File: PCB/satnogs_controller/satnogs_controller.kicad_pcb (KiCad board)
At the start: 2 copper layers, 49.1 x 68 mm, 36 parts, among them P1 RS485, P2 End-Stops, P4 I2C, P5 DC Motors Driver, P6 Power-IN, P7 Motor1, P8 Motor2, P9 Dev-Pins, U1 Pro_Mini, U2 MAX485, U3 POLOLU_A4988, U4 POLOLU_A4988

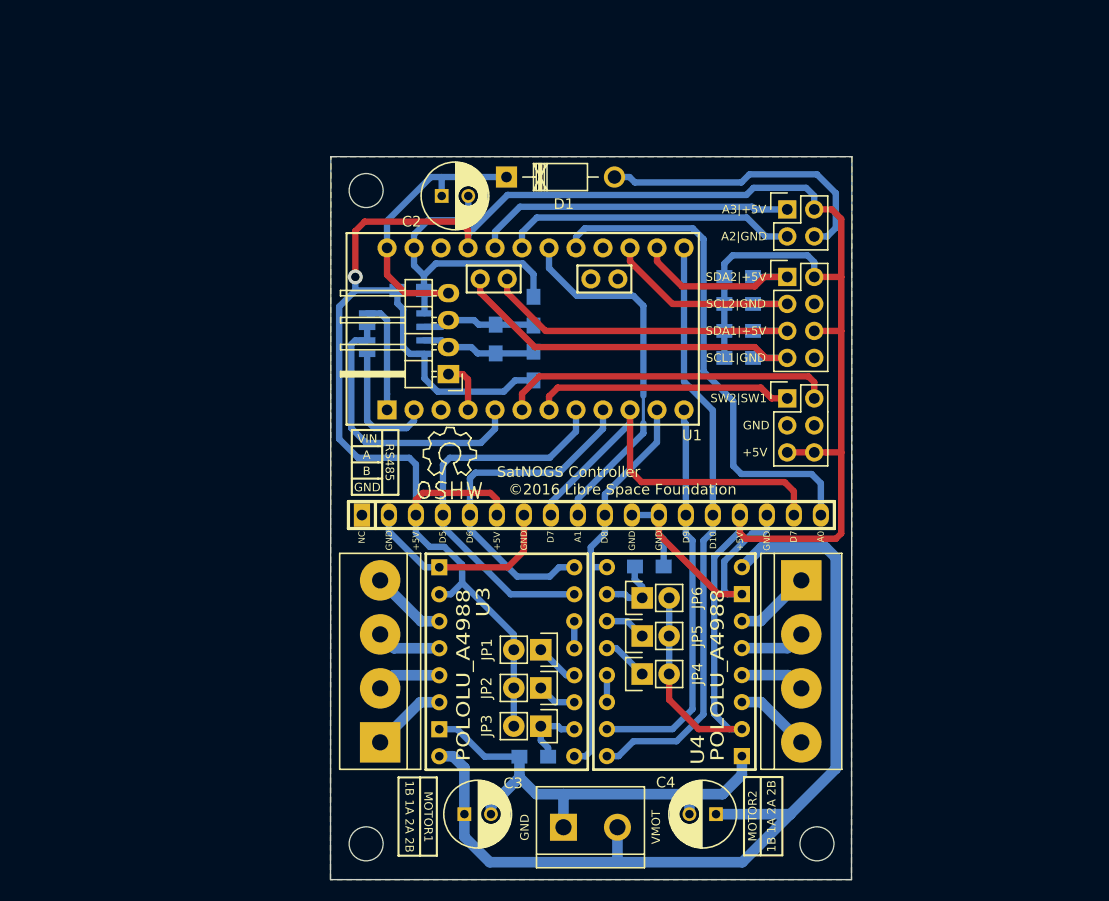
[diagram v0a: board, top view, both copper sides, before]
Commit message: Rotator controller (#27)
* Update satnogs library.

Add new footprints, 3d shapes and schematic components.

* Updates in rotator controller.

Add RJ45 for communication and power in (PoE).
New dimensions of board (euroboard 100x80 mm)
Embed the power supply to the board (WIP).
Add pins for indicator LED and for rf switch (optional).
Add additional pads for power in case that PoE (RJ45) isn't suitable.
Updates in schematic and board wuth new library parts.

* Add PCA9540B schematic component, I2C multiplexer.

* Add fuse holder and stitching via.

* Updates in PCB and schematic.

Add digital and power ground planes (WIP).
Connection of separate GND with zero resistor.
Add I2C multiplexer.
Finalize power supply of 12V.
Change RJ45 to headers.
Add RC filter (LPF) for end-stops.
Add more dev-pins.
Add filter in uC voltage input.

Signed-off-by: zisi <agzisim@gmail.com>

* Add GND-GNDD vias and silkscreen.

Signed-off-by: zisi <agzisim@gmail.com>

* Updates according to Kicad library convention

Signed-off-by: zisi <agzisim@gmail.com>

* Resolve issues #22, #23, #24, #25

Signed-off-by: zisi <agzisim@gmail.com>

* Fix silkscreen placement and zone cleanup

* Use one GND bottom plane and GND areas in front

Remove zero ohm resistors
To avoid connection with GNDD directly with motor GND use keep out area

Signed-off-by: zisi <agzisim@gmail.com>

* Add electrolytic capacitor, TVS-diode in PSU input

Capacitor reduces the voltage ripple of input voltage (long cable)
TVS-diode protect the PSU and all the board from surges and ESD events

Signed-off-by: zisi <agzisim@gmail.com>
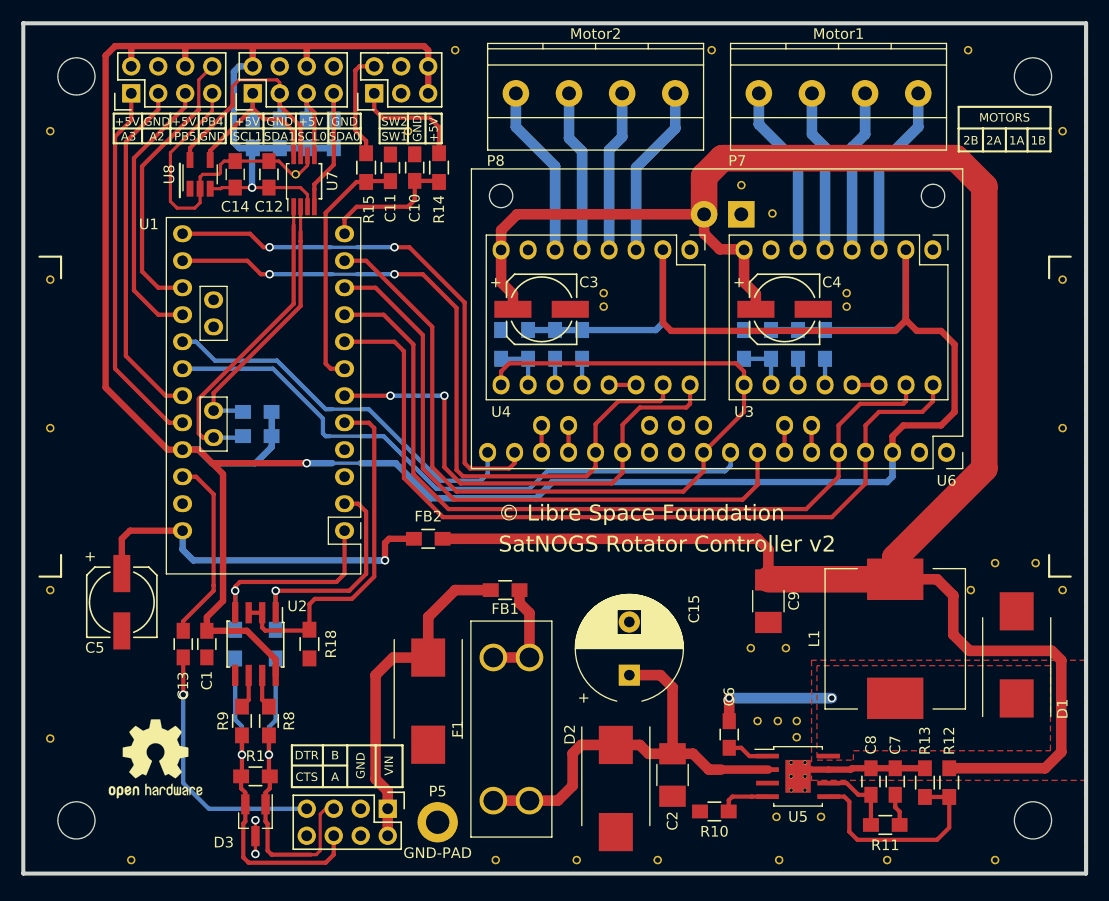
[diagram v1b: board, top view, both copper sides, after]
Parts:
- removed P6: Power-IN, Connect:bornier2
- removed P9: Dev-Pins, Pin_Headers:Pin_Header_Straight_2x02
- removed the REF** at (166.1, 119.1)
- removed the REF** at (123.7, 119.1)
- removed the REF** at (123.7, 57.7)
- removed SatNOGS Controller: ©2016 Libre Space Foundation, Symbols:Symbol_OSHW-Logo_SilkScreen
- added C10: 0.1u, Capacitors_SMD:C_0805_HandSoldering, F.Cu at (128.3, 55.5)
- added C11: 0.1u, Capacitors_SMD:C_0805_HandSoldering, F.Cu at (126.0, 55.5)
- added C12: 0.1u, Capacitors_SMD:C_0805_HandSoldering, F.Cu at (114.6, 56.1)
- added C13: 0.1u, Capacitors_SMD:C_0805_HandSoldering, F.Cu at (106.5, 100.3)
- added C14: 0.1u, Capacitors_SMD:C_0805_HandSoldering, F.Cu at (111.4, 56.1)
- added C15: 100u, satnogs:CP_Radial_D10.0mm_P5.00mm, F.Cu at (148.5, 103.3)
- added C5: 100u, Capacitors_SMD:c_elec_6.3x5.3, F.Cu at (100.7, 96.4)
- added C6: 100n, Capacitors_SMD:C_0805_HandSoldering, F.Cu at (157.9, 108.8)
- added C7: 7.5n, Capacitors_SMD:C_0805_HandSoldering, F.Cu at (173.5, 113.3)
- added C8: 10p, Capacitors_SMD:C_0805_HandSoldering, F.Cu at (171.2, 113.3)
- added C9: 47u, Capacitors_SMD:C_1210_HandSoldering, F.Cu at (161.5, 96.3)
- added D2: D_Schottky, satnogs:DO-214AB_Handsoldering, F.Cu at (147.2, 113.9)
- added D3: D_TVS_x2_AAC, TO_SOT_Packages_SMD:SOT-23_Handsoldering, F.Cu at (113.3, 116.9)
- added D4: D_TVS, satnogs:DO-214AB_Handsoldering, F.Cu at (129.5, 105.7)
- added F1: FUSE, satnogs:FuseHolder_Keystone-3557-10, F.Cu at (137.4, 108.3)
- added FB1: FILTER, Resistors_SMD:R_0805_HandSoldering, F.Cu at (136.8, 95.2)
- added FB2: FILTER, Resistors_SMD:R_0805_HandSoldering, F.Cu at (129.5, 90.4)
- added G***: LOGO, satnogs:satnogs_logo, B.Cu at (156.8, 101.9)
- added JP7: Jumper_NO_Small, Resistors_SMD:R_0805_HandSoldering, B.Cu at (111.4, 100.3)
- added JP8: Jumper_NO_Small, Resistors_SMD:R_0805_HandSoldering, B.Cu at (115.2, 100.3)
- added L1: 27u, satnogs:Inductor_Bourns-SRR1210_HandSoldering, F.Cu at (173.5, 99.8)
- added P3: IN-PINS, Pin_Headers:Pin_Header_Straight_2x04, F.Cu at (125.7, 115.8)
- added R10: 221k, Resistors_SMD:R_0805_HandSoldering, F.Cu at (156.5, 116.1)
- added R11: 26.7k, Resistors_SMD:R_0805_HandSoldering, F.Cu at (172.5, 117.3)
- added R12: 147k, Resistors_SMD:R_0805_HandSoldering, F.Cu at (178.6, 113.4)
- added R13: 10.5k, Resistors_SMD:R_0805_HandSoldering, F.Cu at (176.3, 113.4)
- added R14: 200, Resistors_SMD:R_0805_HandSoldering, F.Cu at (130.6, 55.5)
- added R15: 200, Resistors_SMD:R_0805_HandSoldering, F.Cu at (123.7, 55.5)
- added R16: 4.7k, Resistors_SMD:R_0805_HandSoldering, B.Cu at (113.5, 78.5)
- added R17: 4.7k, Resistors_SMD:R_0805_HandSoldering, B.Cu at (113.5, 80.8)
- added R18: 10k, Resistors_SMD:R_0805_HandSoldering, F.Cu at (118.4, 100.3)
- added REF**: via-0.8mm, satnogs:via-0.8mm, F.Cu at (143.5, 120.7)
- added REF**: via-0.8mm, satnogs:via-0.8mm, F.Cu at (94.0, 66.0)
- added REF**: via-0.8mm, satnogs:via-0.8mm, F.Cu at (94.0, 52.1)
- added REF**: via-0.8mm, satnogs:via-0.8mm, F.Cu at (94.0, 80.0)
- added REF**: via-0.8mm, satnogs:via-0.8mm, F.Cu at (94.0, 95.2)
- added REF**: via-0.8mm, satnogs:via-0.8mm, F.Cu at (94.0, 109.2)
- added REF**: via-0.8mm, satnogs:via-0.8mm, F.Cu at (101.6, 120.7)
- added REF**: via-0.8mm, satnogs:via-0.8mm, F.Cu at (117.1, 56.1)
- added REF**: via-0.8mm, satnogs:via-0.8mm, F.Cu at (160.5, 107.6)
- added REF**: via-0.8mm, satnogs:via-0.8mm, F.Cu at (159.9, 100.7)
- added REF**: via-0.8mm, satnogs:via-0.8mm, F.Cu at (162.4, 107.6)
- added REF**: via-0.8mm, satnogs:via-0.8mm, F.Cu at (164.2, 109.1)
- added REF**: via-0.8mm, satnogs:via-0.8mm, F.Cu at (164.2, 107.6)
- added REF**: via-0.8mm, satnogs:via-0.8mm, F.Cu at (162.3, 116.6)
- added REF**: via-0.8mm, satnogs:via-0.8mm, F.Cu at (163.2, 100.7)
- added REF**: via-0.8mm, satnogs:via-0.8mm, F.Cu at (166.5, 116.6)
- added REF**: via-0.8mm, satnogs:via-0.8mm, F.Cu at (135.9, 120.7)
- added REF**: via-0.8mm, satnogs:via-0.8mm, F.Cu at (162.6, 120.7)
- added REF**: via-0.8mm, satnogs:via-0.8mm, F.Cu at (151.1, 120.7)
- added REF**: via-0.8mm, satnogs:via-0.8mm, F.Cu at (172.7, 120.7)
- added REF**: via-0.8mm, satnogs:via-0.8mm, F.Cu at (182.9, 120.7)
- added REF**: via-0.8mm, satnogs:via-0.8mm, F.Cu at (189.2, 95.2)
- added REF**: via-0.8mm, satnogs:via-0.8mm, F.Cu at (180.6, 95.2)
- added REF**: via-0.8mm, satnogs:via-0.8mm, F.Cu at (156.2, 44.5)
- added REF**: via-0.8mm, satnogs:via-0.8mm, F.Cu at (180.3, 44.5)
- added REF**: via-0.8mm, satnogs:via-0.8mm, F.Cu at (189.2, 52.1)
- added REF**: via-0.8mm, satnogs:via-0.8mm, F.Cu at (168.9, 68.6)
- added REF**: via-0.8mm, satnogs:via-0.8mm, F.Cu at (189.2, 66.0)
- added REF**: via-0.8mm, satnogs:via-0.8mm, F.Cu at (159.0, 57.1)
- added REF**: via-0.8mm, satnogs:via-0.8mm, F.Cu at (146.1, 68.6)
- added REF**: via-0.8mm, satnogs:via-0.8mm, F.Cu at (189.2, 80.0)
- added REF**: via-0.8mm, satnogs:via-0.8mm, F.Cu at (127.6, 52.1)
- added REF**: via-0.8mm, satnogs:via-0.8mm, F.Cu at (186.7, 92.7)
- added REF**: via-0.8mm, satnogs:via-0.8mm, F.Cu at (182.9, 92.7)
- added REF**: via-0.8mm, satnogs:via-0.8mm, F.Cu at (168.9, 67.3)
- added REF**: via-0.8mm, satnogs:via-0.8mm, F.Cu at (146.1, 67.3)
- added REF**: via-0.8mm, satnogs:via-0.8mm, F.Cu at (161.9, 59.8)
- added REF**: via-0.8mm, satnogs:via-0.8mm, F.Cu at (132.1, 44.5)
- added REF***: OSHW-Logo2_9.8x8mm_SilkScreen, Symbols:OSHW-Logo2_9.8x8mm_SilkScreen, F.Cu at (103.9, 111.1)
- added U5: TPS54360DDA, satnogs:HSOP-8, F.Cu at (164.3, 112.8)
- added U6: Pololu_Dual_MC33926, satnogs:Pololu_Dual_MC33926, F.Cu at (178.3, 82.3)
- added U7: PCA9540B, satnogs:TSSOP-8_3x3mm_Pitch0.65mm_HandSoldering, F.Cu at (117.9, 56.8)
- added U8: TC74, satnogs:SOT-23-5_HandSoldering, F.Cu at (108.1, 56.1)
- added © Libre Space Foundation: EuroBoard_halb_Type-I_100mmX80mm_holes, EuroBoard_Outline:EuroBoard_halb_Type-I_100mmX80mm_holes, F.Cu at (91.4, 121.9)
- C1, R1: moved to F.Cu
- C2: value 10u -> 2.2u; footprint Capacitors_ThroughHole:C_Radial_D6.3_L11.2_P2.5 -> Capacitors_SMD:C_1210_HandSoldering
- C3, C4: footprint Capacitors_ThroughHole:C_Radial_D6.3_L11.2_P2.5 -> Capacitors_SMD:c_elec_6.3x5.3
- D1: value ZENERsmall -> D_Schottky; footprint Diodes_ThroughHole:Diode_DO-41_SOD81_Horizontal_RM10 -> satnogs:DO-214AB_Handsoldering
- JP1, JP2, JP3, JP4, JP5, JP6: footprint Pin_Headers:Pin_Header_Straight_1x02 -> Resistors_SMD:R_0805_HandSoldering; moved to B.Cu
- P1: value RS485 -> DEV-PINS; footprint Pin_Headers:Pin_Header_Angled_1x04 -> Pin_Headers:Pin_Header_Straight_2x04
- P5: value DC Motors Driver -> GND-PAD; footprint satnogs:pin_socket_18 -> Mounting_Holes:MountingHole_2.2mm_M2_DIN965_Pad
- P7, P8: footprint Connect:bornier4 -> satnogs:MKDS_1.5-4
- R8, R9: value 4.7k -> 10; moved to F.Cu
- U1: value Pro_Mini -> Arduino_Pro_Mini; footprint satnogs:pro-mini -> satnogs:Arduino_Pro_Mini
- U2: value MAX485 -> SN65HVD485EDR; footprint Housings_SOIC:SOIC-8_3.9x4.9mm_Pitch1.27mm -> satnogs:SOIC-8_3.9x4.9mm_Pitch1.27mm_HandSoldering; moved to F.Cu
- U3, U4: value POLOLU_A4988 -> Pololu_A4988; footprint satnogs:SWDIP8_.6W -> satnogs:Pololu_A4988
- moved P7 68.7 mm to (168.1, 48.5), turned to 180 degrees
- moved D1 65.8 mm to (184.9, 101.3), turned to 90 degrees
- moved C2 58.7 mm to (152.5, 112.6), turned to 270 degrees
- moved P8 56.8 mm to (145.3, 48.5), turned to 180 degrees
- moved U3 55.8 mm to (177.0, 63.2)
- moved P4 53.2 mm to (113.0, 48.5), turned to 90 degrees
- moved R6 48.4 mm to (113.0, 52.3), turned to 90 degrees
- moved P2 48.3 mm to (124.5, 48.5), turned to 90 degrees
- moved C3 48.1 mm to (140.2, 68.8)
- moved C4 47.9 mm to (163.1, 68.8), turned to 0 degrees
- moved R9 47.3 mm to (112.0, 107.6)
- moved R1 46.9 mm to (113.3, 112.8), turned to 180 degrees
- moved R3 45.8 mm to (118.1, 52.3), turned to 90 degrees
- moved R5 45.2 mm to (115.6, 52.3), turned to 90 degrees
- moved R4 43.5 mm to (159.3, 72.1), turned to 90 degrees
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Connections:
- net /VMOT renamed +12V
- net Net-(JP1-Pad1) renamed /MS3M1
- net Net-(JP2-Pad1) renamed /MS2M1
- net Net-(JP4-Pad1) renamed /MS3M2
- net Net-(JP5-Pad1) renamed /MS2M2
- net Net-(U3-Pad13) renamed /M1RST
- net Net-(U4-Pad13) renamed /M2RST
- C1 pad 1: GND -> +5V
- C1 pad 2: +5V -> GND
- C2 pad 1: /VIN -> /SW_VIN
- D1 pad 1: /VIN -> /SW
- P1 pad 1: GND -> /A3
- P1 pad 2: /B -> +5V
- P1 pad 3: /A -> /A2
- P1 pad 4: /VIN -> GND
- P2 pad 1: /SW2 -> Net-(P2-Pad1)
- P2 pad 2: /SW1 -> Net-(P2-Pad2)
- P4 pad 1: /SDA2 -> /SCL1
- P4 pad 3: /SCL2 -> /SDA1
- P4 pad 5: /SDA1 -> /SCL0
- P4 pad 7: /SCL1 -> /SDA0
- P5 pad 1: Net-(P5-Pad1) -> GND
- P7 pad 1: /2BM1 -> /1BM1
- P7 pad 2: /2AM1 -> /1AM1
- P7 pad 3: /1AM1 -> /2AM1
- P7 pad 4: /1BM1 -> /2BM1
- P8 pad 1: /2BM2 -> /1BM2
- P8 pad 2: /2AM2 -> /1AM2
- P8 pad 3: /1AM2 -> /2AM2
- P8 pad 4: /1BM2 -> /2BM2
- R1 pad 1: /A -> /B
- R1 pad 2: /B -> /A
- R2 pad 2: /SDA1 -> /SDA0
- R3 pad 2: /SCL1 -> /SCL0
- R5 pad 2: /SDA2 -> /SDA1
- R6 pad 2: /SCL2 -> /SCL1
- R8 pad 1: +5V -> Net-(R8-Pad1)
- R9 pad 2: GND -> Net-(R9-Pad2)
- U1 pad 10: /SF -> /M1SF
- U1 pad 12: /M2IN2 -> /SW1
- U1 pad 13: /M2IN1 -> /M2SF
- U1 pad 14: /SDA2 -> /M2IN1
- U1 pad 15: /SCL2 -> /PB4
- U1 pad 16: Net-(U1-Pad16) -> /PB5
- U1 pad 23: /SDA1 -> /SDA
- U1 pad 24: /SCL1 -> /SCL
- U1 pad 28: /VIN -> Net-(C5-Pad1)
- U1 pad 6: /SW1 -> /M2IN2
- U2 pad 6: /A -> Net-(R9-Pad2)
- U2 pad 7: /B -> Net-(R8-Pad1)
- U3 pad 15: /M1IN2 -> /M1IN1
- U3 pad 16: /M1IN1 -> /M1IN2
- U4 pad 15: /M2IN2 -> /M2IN1
- U4 pad 16: /M2IN1 -> /M2IN2
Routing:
- net GND: track 157.0 -> 47.0 mm, vias 0 -> 2
- net +12V: track 89.0 -> 198.6 mm
- net +5V: track 261.7 -> 323.5 mm, vias 1 -> 2
- net /M1SF: track 0.00 -> 58.1 mm
- net /M2SF: track 0.00 -> 50.5 mm, vias 0 -> 2
- net /EN: track 38.3 -> 87.0 mm
- net /M1IN1: track 33.4 -> 76.1 mm
- net /M1IN2: track 36.7 -> 78.5 mm
- net /SW_VIN: track 0.00 -> 41.6 mm
- net /SF: track 37.3 -> 0.00 mm
- net Net-(C5-Pad1): track 0.00 -> 35.1 mm, vias 0 -> 1
- net /SCL: track 0.00 -> 29.4 mm
- net /PB4: track 0.00 -> 26.5 mm
- net /PB5: track 0.00 -> 26.1 mm
- net /SDA: track 0.00 -> 25.4 mm
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- added copper zone on F.Cu, net /SW
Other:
- board size 49.1 x 68 mm -> 100 x 80 mm
- net class Default: via_dia 1.4 -> 0.8; via_drill 0.8 -> 0.5
- net class neck added: clearance 0.2, trace_width 0.3, via_dia 0.8, via_drill 0.5
- net class power1 added: clearance 0.2, trace_width 0.6, via_dia 0.8, via_drill 0.5
- net class power2 added: clearance 0.6, trace_width 1, via_dia 0.8, via_drill 0.5
- net class signal added: clearance 0.2, trace_width 0.4, via_dia 0.8, via_drill 0.5
- rule trace_min: 0.2 -> 0.15
- rule via_min_drill: 0.3 -> 0.35
- board text added: "A2"
- board text added: "A3"
- board text added: "CTS"
- board text added: "DTR"
- board text added: "MOTORS"
- board text added: "PB4"
- board text added: "PB5"
- board text added: "SCL0"
- board text added: "SCL1"
- board text added: "SDA0"
- board text added: "SDA1"
- board text added: "SW1"
- board text added: "SW2"
- board text added: "SatNOGS Rotator Controller v2"
- board text removed: "A0"
- board text removed: "A1"
- board text removed: "D10"
- board text removed: "D5"
- board text removed: "D6"
- board text removed: "D7"
- board text removed: "D8"
- board text removed: "D9"
- board text removed: "MOTOR1"
- board text removed: "MOTOR2"
- board text removed: "NC"
- board text removed: "RS485"
- board text removed: "SCL1|GND"
- board text removed: "SCL2|GND"
- board text removed: "SDA1|+5V"
- board text removed: "SDA2|+5V"
- board text removed: "SW2|SW1"
- board text removed: "VMOT"
- board text removed: "Α2|GND"
- board text removed: "Α3|+5V"
